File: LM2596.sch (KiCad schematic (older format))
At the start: 10 parts

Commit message: исправление согласно замечаниям, переразведена PL2303
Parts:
- added C20: 470uF, Capacitors_ThroughHole:C_Radial_D7.5_L11.2_P2.5, symbol C
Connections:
- wire segments 24 -> 26
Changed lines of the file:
@@
 	2800 3450 3100 3450
 Wire Wire Line
-	3900 4100 6350 4100
+	3065 4100 6350 4100
 Wire Wire Line
 	8200 4255 8200 4310
@@
 Wire Wire Line
 	8200 3755 9000 3755
+$Comp
+L C C20
+U 1 1 5756A584
+P 3065 3675
+F 0 "C20" H 3090 3775 50  0000 L CNN
+F 1 "470uF" H 3090 3575 50  0000 L CNN
+F 2 "Capacitors_ThroughHole:C_Radial_D7.5_L11.2_P2.5" H 3103 3525 50  0001 C CNN
+F 3 "" H 3065 3675 50  0000 C CNN
+	1    3065 3675
+	1    0    0    -1
+$EndComp
+Wire Wire Line
+	3065 3525 3065 3450
+Connection ~ 3065 3450
+Wire Wire Line
+	3065 3825 3065 4100
 $EndSCHEMATC

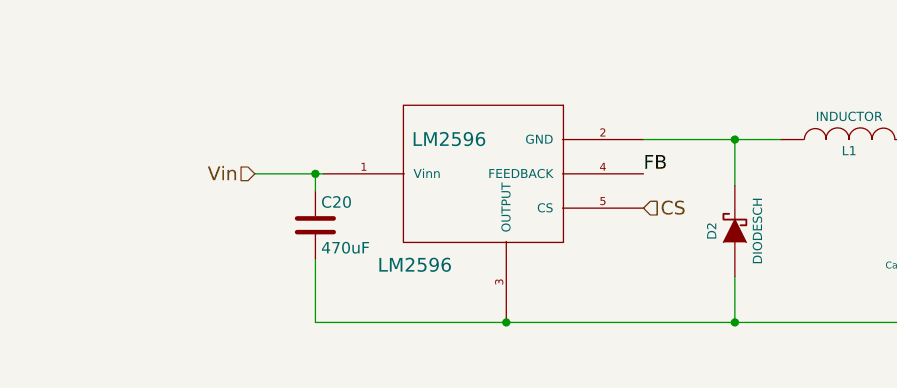
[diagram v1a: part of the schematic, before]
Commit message: подключение питания LMки от USB
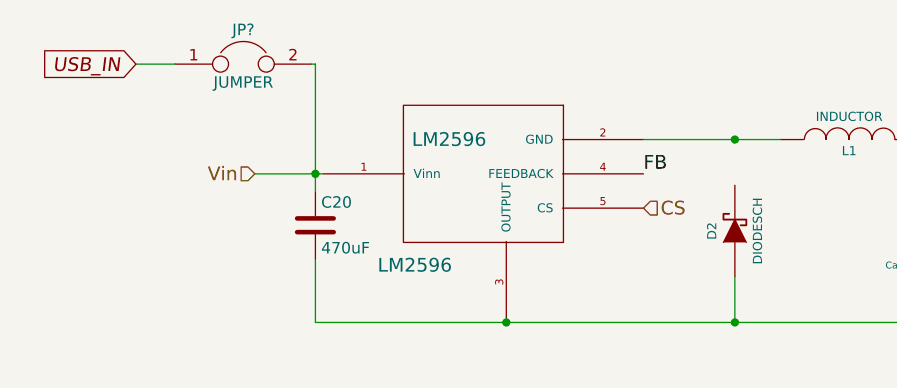
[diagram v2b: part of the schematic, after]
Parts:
- added JP?: JUMPER, symbol JUMPER
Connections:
- net labels added: USB_IN
- wire segments 26 -> 27
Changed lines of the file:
@@
 LIBS:Pulse_Module-rescue
 LIBS:conn3
+LIBS:pl2303
 LIBS:power
 LIBS:device
@@
 	4900 4100 4900 3900
 Connection ~ 3900 4100
-Wire Wire Line
-	4900 3500 4900 3300
 Connection ~ 4900 3300
 Wire Wire Line
@@
 $EndComp
 Wire Wire Line
-	3065 3525 3065 3450
+	3065 2970 3065 3525
 Connection ~ 3065 3450
 Wire Wire Line
 	3065 3825 3065 4100
+$Comp
+L JUMPER JP?
+U 1 1 577BC04B
+P 2750 2970
+F 0 "JP?" H 2750 3120 50  0000 C CNN
+F 1 "JUMPER" H 2750 2890 50  0000 C CNN
+F 2 "" H 2750 2970 50  0000 C CNN
+F 3 "" H 2750 2970 50  0000 C CNN
+	1    2750 2970
+	1    0    0    -1
+$EndComp
+Wire Wire Line
+	3065 2970 3050 2970
+Wire Wire Line
+	2450 2970 2280 2970
+Text GLabel 2280 2970 0    60   Input Italic 0
+USB_IN
 $EndSCHEMATC

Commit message: разделение питания и добавление потенциометра у лмки
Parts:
- removed JP2: JUMPER3, Connect:PINHEAD1-3, symbol JUMPER3
- removed R14, R15: 1k, Resistors_SMD:R_0805, symbol R
- removed R9: R, Resistors_SMD:R_0805, symbol R
- added RV?: POT, symbol POT
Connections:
- wire segments 27 -> 20
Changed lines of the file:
@@
-$EndComp
-$Comp
-L R R14
-U 1 1 572B2DAD
-P 8040 3460
-F 0 "R14" V 8120 3460 50  0000 C CNN
-F 1 "1k" V 8040 3460 50  0000 C CNN
-F 2 "Resistors_SMD:R_0805" V 7970 3460 50  0001 C CNN
-F 3 "" H 8040 3460 50  0000 C CNN
-	1    8040 3460
-	1    0    0    -1
-$EndComp
-$Comp
-L R R15
-U 1 1 572B2E55
-P 8200 4460
-F 0 "R15" V 8280 4460 50  0000 C CNN
-F 1 "1k" V 8200 4460 50  0000 C CNN
-F 2 "Resistors_SMD:R_0805" V 8130 4460 50  0001 C CNN
-F 3 "" H 8200 4460 50  0000 C CNN
-	1    8200 4460
-	1    0    0    -1
-$EndComp
-$Comp
-L R R9
-U 1 1 5740479F
-P 9000 4460
-F 0 "R9" V 9080 4460 50  0000 C CNN
-F 1 "R" V 9000 4460 50  0000 C CNN
-F 2 "Resistors_SMD:R_0805" V 8930 4460 50  0001 C CNN
-F 3 "" H 9000 4460 50  0000 C CNN
-	1    9000 4460
-	1    0    0    -1
-$EndComp
-$Comp
-L JUMPER3 JP2
-U 1 1 5740CAA4
-P 8200 4005
-F 0 "JP2" H 8250 3905 50  0000 L CNN
-F 1 "JUMPER3" H 8200 4105 50  0000 C BNN
-F 2 "Connect:PINHEAD1-3" H 8200 4005 50  0001 C CNN
-F 3 "" H 8200 4005 50  0000 C CNN
-	1    8200 4005
-	0    1    1    0
 $EndComp
 $Comp
 L GND #PWR037
 U 1 1 57477506
-P 8625 4755
-F 0 "#PWR037" H 8625 4505 50  0001 C CNN
-F 1 "GND" H 8625 4605 50  0000 C CNN
-F 2 "" H 8625 4755 50  0000 C CNN
-F 3 "" H 8625 4755 50  0000 C CNN
-	1    8625 4755
+P 8190 3940
+F 0 "#PWR037" H 8190 3690 50  0001 C CNN
+F 1 "GND" H 8190 3790 50  0000 C CNN
+F 2 "" H 8190 3940 50  0000 C CNN
+F 3 "" H 8190 3940 50  0000 C CNN
+	1    8190 3940
 	1    0    0    -1
 $EndComp
@@
 	7750 3150 7750 3300
 Wire Wire Line
-	6350 3150 8040 3150
+	6350 3150 8190 3150
 Connection ~ 6350 3300
 Connection ~ 7750 3150
@@
 	3065 4100 6350 4100
 Wire Wire Line
-	8200 4255 8200 4310
-Wire Wire Line
-	8200 4610 8200 4680
-Wire Wire Line
-	8200 4680 9000 4680
-Wire Wire Line
-	9000 4680 9000 4610
-Wire Wire Line
-	9000 3755 9000 4310
-Wire Wire Line
-	8625 4680 8625 4755
-Connection ~ 8625 4680
-Wire Wire Line
-	8040 3150 8040 3310
-Wire Wire Line
-	8040 3610 8040 4005
-Wire Wire Line
-	8040 4005 8100 4005
-Wire Wire Line
 	7425 3700 8040 3700
-Connection ~ 8040 3700
 Wire Wire Line
 	7750 3600 7750 3700
 Connection ~ 7750 3700
-Wire Wire Line
-	8200 3755 9000 3755
 $Comp
 L C C20
@@
 Text GLabel 2280 2970 0    60   Input Italic 0
 USB_IN
+Wire Wire Line
+	4900 3295 4900 3500
+$Comp
+L POT RV?
+U 1 1 578E6F94
+P 8190 3700
+F 0 "RV?" V 8190 3620 50  0000 C CNN
+F 1 "POT" H 8190 3700 50  0000 C CNN
+F 2 "" H 8190 3700 50  0000 C CNN
+F 3 "" H 8190 3700 50  0000 C CNN
+	1    8190 3700
+	0    -1   -1   0
+$EndComp
+Wire Wire Line
+	8190 3150 8190 3550
+Wire Wire Line
+	8190 3850 8190 3940
 $EndSCHEMATC

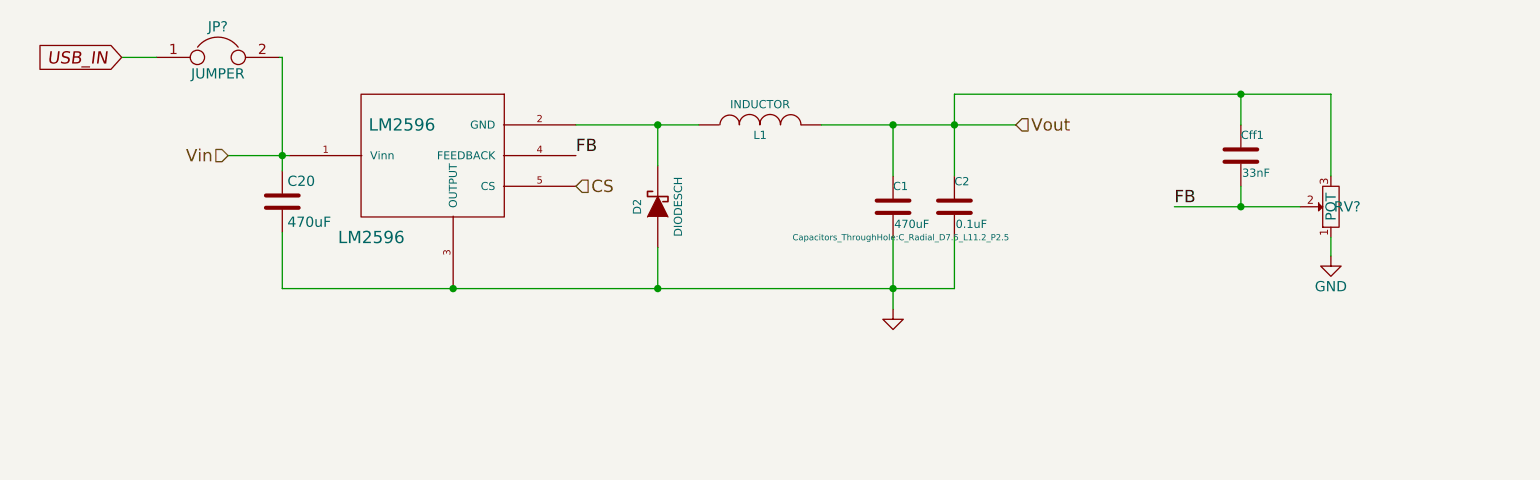
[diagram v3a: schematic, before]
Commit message: Добавлен AMS1117 и изменения в питании
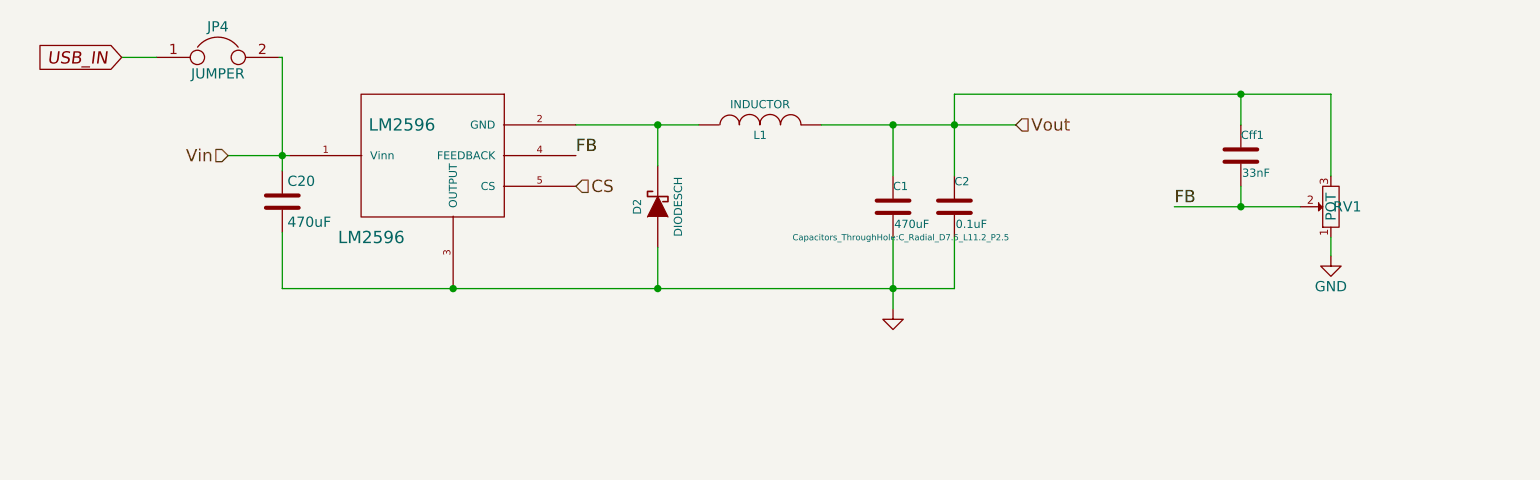
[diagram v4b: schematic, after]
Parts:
- JP4: renamed from JP?; footprint (none) -> Connect:PINHEAD1-2
- gave numbers to parts that had none: 1
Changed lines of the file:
@@
 Vout
 $Comp
-L GND #PWR036
+L GND #PWR05
 U 1 1 56DED666
 P 6050 4200
-F 0 "#PWR036" H 6050 4200 30  0001 C CNN
+F 0 "#PWR05" H 6050 4200 30  0001 C CNN
 F 1 "GND" H 6050 4130 30  0001 C CNN
 F 2 "" H 6050 4200 60  0000 C CNN
@@
 $EndComp
 $Comp
-L GND #PWR037
+L GND #PWR06
 U 1 1 57477506
 P 8190 3940
-F 0 "#PWR037" H 8190 3690 50  0001 C CNN
+F 0 "#PWR06" H 8190 3690 50  0001 C CNN
 F 1 "GND" H 8190 3790 50  0000 C CNN
 F 2 "" H 8190 3940 50  0000 C CNN
@@
 	3065 3825 3065 4100
 $Comp
-L JUMPER JP?
+L JUMPER JP4
 U 1 1 577BC04B
 P 2750 2970
-F 0 "JP?" H 2750 3120 50  0000 C CNN
+F 0 "JP4" H 2750 3120 50  0000 C CNN
 F 1 "JUMPER" H 2750 2890 50  0000 C CNN
-F 2 "" H 2750 2970 50  0000 C CNN
+F 2 "Connect:PINHEAD1-2" H 2750 2970 50  0001 C CNN
 F 3 "" H 2750 2970 50  0000 C CNN
 	1    2750 2970
@@
 	4900 3295 4900 3500
 $Comp
-L POT RV?
+L POT RV1
 U 1 1 578E6F94
 P 8190 3700
-F 0 "RV?" V 8190 3620 50  0000 C CNN
+F 0 "RV1" V 8190 3620 50  0000 C CNN
 F 1 "POT" H 8190 3700 50  0000 C CNN
-F 2 "" H 8190 3700 50  0000 C CNN
+F 2 "" H 8190 3700 50  0001 C CNN
 F 3 "" H 8190 3700 50  0000 C CNN
 	1    8190 3700

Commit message: Изменения футпринтов
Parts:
- RV1: footprint (none) -> Potentiometers:Potentiometer_Alps-RK163-single_15mm
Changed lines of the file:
@@
 LIBS:contrib
 LIBS:valves
+LIBS:AMS1117
 LIBS:Pulse_Module-cache
 EELAYER 25 0
@@
 Vout
 $Comp
-L GND #PWR05
+L GND #PWR06
 U 1 1 56DED666
 P 6050 4200
-F 0 "#PWR05" H 6050 4200 30  0001 C CNN
+F 0 "#PWR06" H 6050 4200 30  0001 C CNN
 F 1 "GND" H 6050 4130 30  0001 C CNN
 F 2 "" H 6050 4200 60  0000 C CNN
@@
 $EndComp
 $Comp
-L GND #PWR06
+L GND #PWR07
 U 1 1 57477506
 P 8190 3940
-F 0 "#PWR06" H 8190 3690 50  0001 C CNN
+F 0 "#PWR07" H 8190 3690 50  0001 C CNN
 F 1 "GND" H 8190 3790 50  0000 C CNN
 F 2 "" H 8190 3940 50  0000 C CNN
@@
 F 0 "RV1" V 8190 3620 50  0000 C CNN
 F 1 "POT" H 8190 3700 50  0000 C CNN
-F 2 "" H 8190 3700 50  0001 C CNN
+F 2 "Potentiometers:Potentiometer_Alps-RK163-single_15mm" H 8190 3700 50  0001 C CNN
 F 3 "" H 8190 3700 50  0000 C CNN
 	1    8190 3700

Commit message: Последние изменения
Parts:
- RV1: footprint Potentiometers:Potentiometer_Alps-RK163-single_15mm -> Potentiometers:Potentiometer_Bourns_3296W_3-8Zoll_Inline_ScrewUp
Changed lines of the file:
@@
 Vout
 $Comp
-L GND #PWR06
+L GND #PWR03
 U 1 1 56DED666
 P 6050 4200
-F 0 "#PWR06" H 6050 4200 30  0001 C CNN
+F 0 "#PWR03" H 6050 4200 30  0001 C CNN
 F 1 "GND" H 6050 4130 30  0001 C CNN
 F 2 "" H 6050 4200 60  0000 C CNN
@@
 $EndComp
 $Comp
-L GND #PWR07
+L GND #PWR04
 U 1 1 57477506
 P 8190 3940
-F 0 "#PWR07" H 8190 3690 50  0001 C CNN
+F 0 "#PWR04" H 8190 3690 50  0001 C CNN
 F 1 "GND" H 8190 3790 50  0000 C CNN
 F 2 "" H 8190 3940 50  0000 C CNN
@@
 F 0 "RV1" V 8190 3620 50  0000 C CNN
 F 1 "POT" H 8190 3700 50  0000 C CNN
-F 2 "Potentiometers:Potentiometer_Alps-RK163-single_15mm" H 8190 3700 50  0001 C CNN
+F 2 "Potentiometers:Potentiometer_Bourns_3296W_3-8Zoll_Inline_ScrewUp" H 8190 3700 50  0001 C CNN
 F 3 "" H 8190 3700 50  0000 C CNN
 	1    8190 3700
